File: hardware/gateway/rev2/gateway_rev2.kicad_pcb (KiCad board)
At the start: 2 copper layers, 94 x 78 mm, 68 parts, among them IC1 STM8L151K4T6, IC2 CC1101RGPR, IC5 MB85RC64TAPNF-G-BDERE1, J1 22-28-4044, J2 M20-9770342, U1 IRM-01-3.3, Y1 NX3225GA-26MHZ-TI

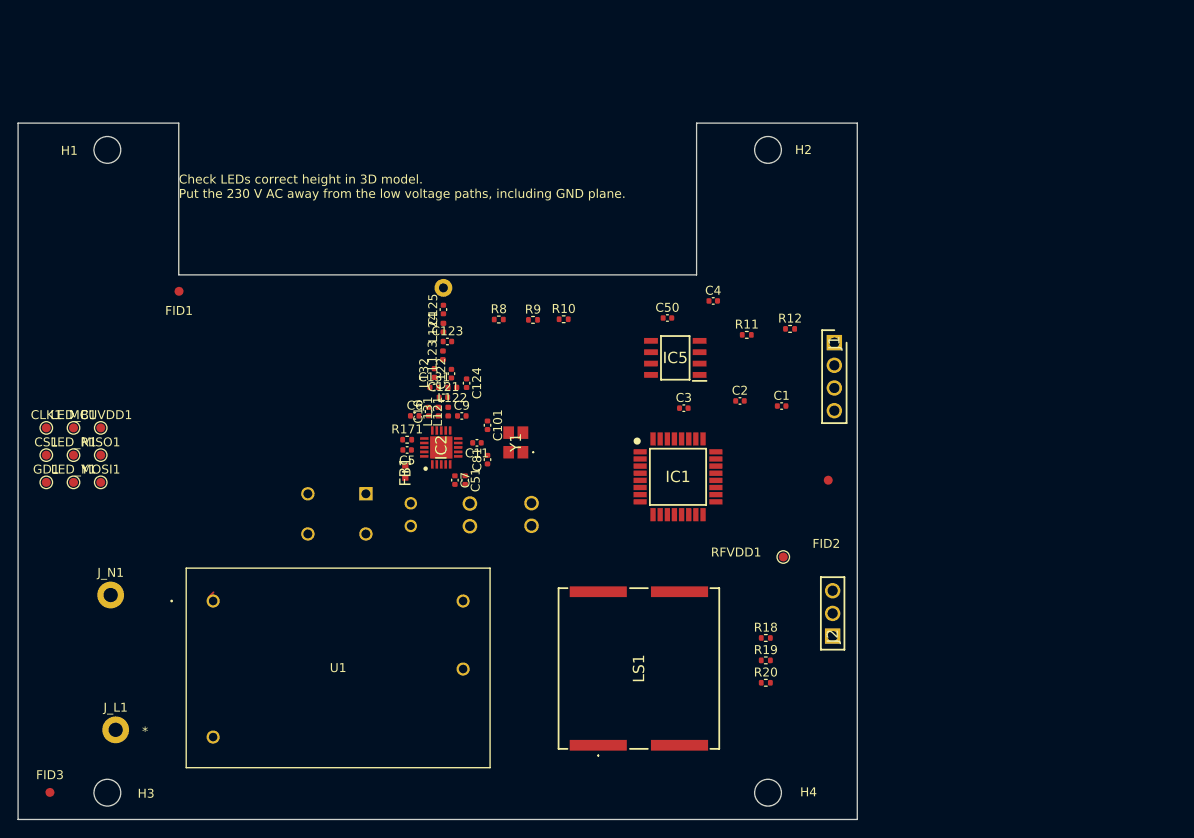
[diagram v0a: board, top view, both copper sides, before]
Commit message: EG-59 RF connected.
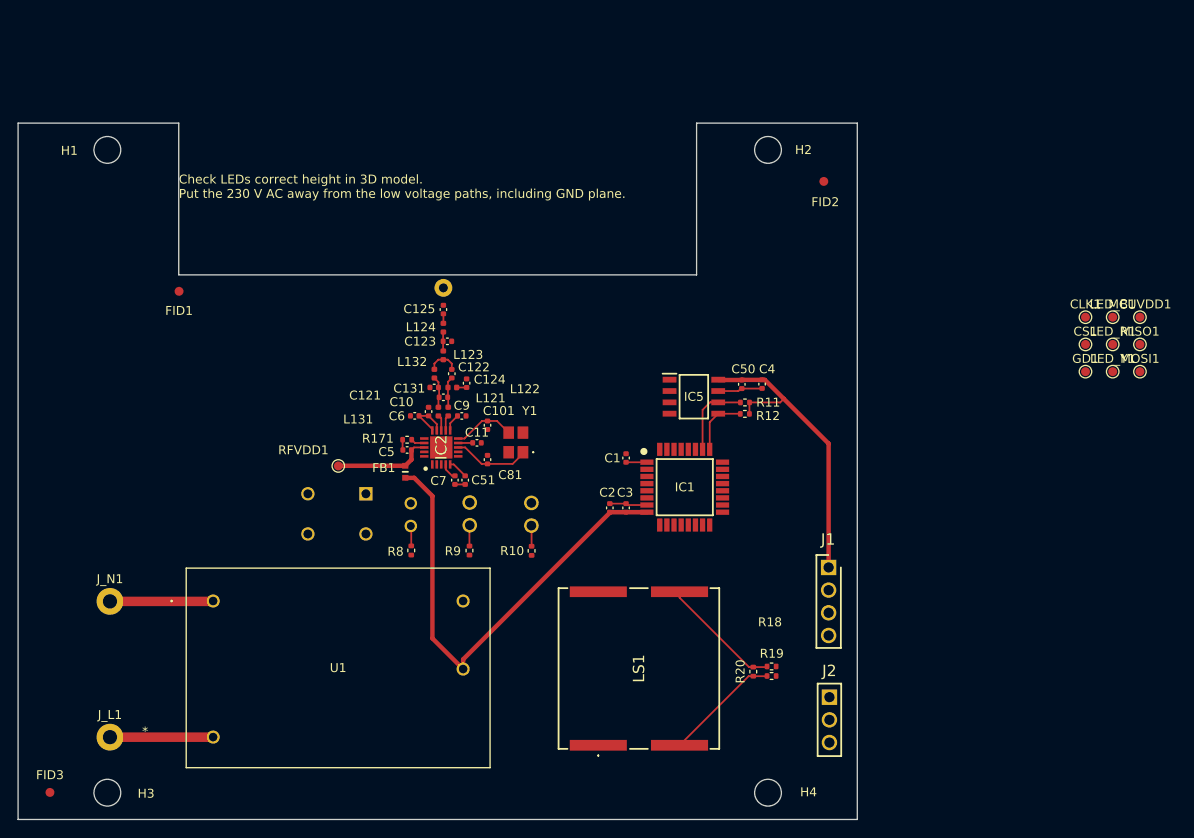
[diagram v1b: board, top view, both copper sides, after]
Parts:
- moved MCUVDD1 117.1 mm to (305.7, 101.7)
- moved MISO1 117.1 mm to (305.7, 104.8)
- moved MOSI1 117.1 mm to (305.7, 107.8)
- moved CLK1 117.1 mm to (299.6, 101.7)
- moved LED_B1 117.1 mm to (302.6, 101.7)
- moved CS1 117.1 mm to (299.6, 104.8)
- moved GD1 117.1 mm to (299.6, 107.8)
- moved LED_R1 117.1 mm to (302.6, 104.8)
- moved LED_Y1 117.1 mm to (302.6, 107.8)
- moved RFVDD1 50.9 mm to (215.9, 118.4)
- moved FID2 33.5 mm to (270.2, 86.5)
- moved R8 27.7 mm to (224.0, 127.9), turned to 90 degrees
- moved R9 26.8 mm to (230.6, 127.9), turned to 90 degrees
- moved R10 26.2 mm to (237.5, 127.9), turned to 90 degrees
- moved J1 25.2 mm to (270.8, 129.8)
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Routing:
- net VDD: track 0.00 -> 87.7 mm
- net RF_VDD: track 0.00 -> 21.9 mm
- net Net-(LS1--_1): track 0.00 -> 13.7 mm
- net Net-(LS1-+_1): track 0.00 -> 13.0 mm
- net GND: track 0.00 -> 11.6 mm
- net Net-(J_L1-V): track 0.00 -> 11.6 mm
- net Net-(J_N1-V): track 0.64 -> 11.6 mm
- net SCL: track 0.00 -> 9.02 mm
- net Net-(IC2-XOSC_Q1): track 0.00 -> 8.64 mm
- net Net-(IC2-XOSC_Q2): track 0.00 -> 7.01 mm
- net SDA: track 0.00 -> 6.87 mm
- net Net-(C122-Pad2): track 0.00 -> 3.61 mm
- net Net-(C121-Pad2): track 0.00 -> 3.53 mm
- net Net-(C121-Pad1): track 0.00 -> 3.49 mm
- net Net-(LED2-A): track 0.00 -> 2.34 mm
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
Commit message: EG-59 MCU almost connected to the RF chip.
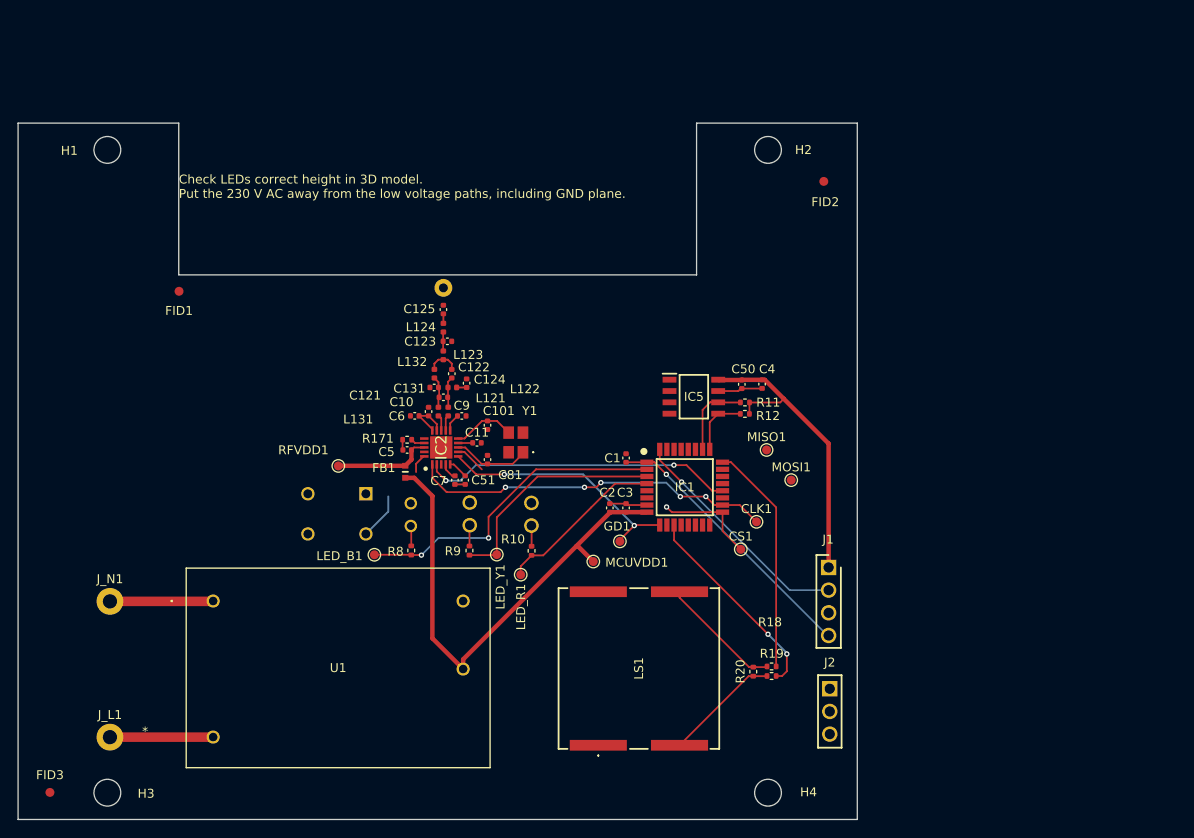
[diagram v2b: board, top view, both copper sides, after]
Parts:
- moved LED_B1 86.9 mm to (219.9, 128.3)
- moved LED_Y1 72.0 mm to (233.6, 128.3)
- moved LED_R1 71.1 mm to (236.3, 130.6)
- moved MCUVDD1 67.1 mm to (244.4, 129.1)
- moved GD1 55.5 mm to (247.4, 126.8)
- moved CS1 44.9 mm to (260.9, 127.7)
- moved MISO1 43.5 mm to (263.8, 116.6)
- moved CLK1 43.4 mm to (262.7, 124.7)
- moved MOSI1 40.9 mm to (266.6, 120.0)
- moved J2 0.94 mm to (270.9, 143.4)
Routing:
- net /MCU/SCLK: track 0.00 -> 40.7 mm, vias 0 -> 5
- net LED_B: track 0.00 -> 35.9 mm, vias 0 -> 2
- net /MCU/SDO: track 0.00 -> 35.1 mm, vias 0 -> 2
- net NRST: track 2.34 -> 30.7 mm, vias 0 -> 1
- net /MCU/IRQ: track 0.00 -> 28.2 mm, vias 0 -> 2
- net SWIM: track 0.00 -> 26.2 mm, vias 0 -> 1
- net LED_Y: track 0.00 -> 26.0 mm
- net BZR_N: track 0.00 -> 25.9 mm
- net BZR_P: track 0.00 -> 23.0 mm, vias 0 -> 2
- net LED_R: track 0.00 -> 18.9 mm
- net /MCU/CS: track 0.00 -> 15.0 mm, vias 0 -> 1
- net BTN: track 0.00 -> 5.25 mm
- net VDD: track 87.7 -> 90.3 mm
- net /MCU/SDI: track 0.00 -> 2.19 mm

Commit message: EG-59 All components connected except GND.
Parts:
- moved J1 29.2 mm to (271.4, 100.6)
- moved J2 24.6 mm to (271.4, 118.7), turned to 90 degrees
- moved CS1 0.91 mm to (261.0, 126.8)
- moved MOSI1 0.67 mm to (265.9, 120.2)
- moved MISO1 0.39 mm to (263.6, 116.9)
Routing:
- net BTN: track 5.25 -> 54.5 mm, vias 0 -> 1
- net /MCU/SDI: track 2.19 -> 44.6 mm, vias 0 -> 2
- net VDD: track 90.3 -> 125.2 mm
- net /MCU/CS: track 15.0 -> 38.0 mm, vias 1 -> 2
- net /MCU/IRQ: track 28.2 -> 5.31 mm, vias 2 -> 1
- net TX: track 0.00 -> 18.5 mm, vias 0 -> 1
- net RX: track 0.00 -> 18.2 mm, vias 0 -> 1
- net /MCU/SDO: track 35.1 -> 42.4 mm
- net NRST: track 30.7 -> 28.3 mm
- net /MCU/SCLK: track 40.7 -> 40.0 mm, vias 5 -> 2
- net BZR_N: track 25.9 -> 26.2 mm, vias 0 -> 2

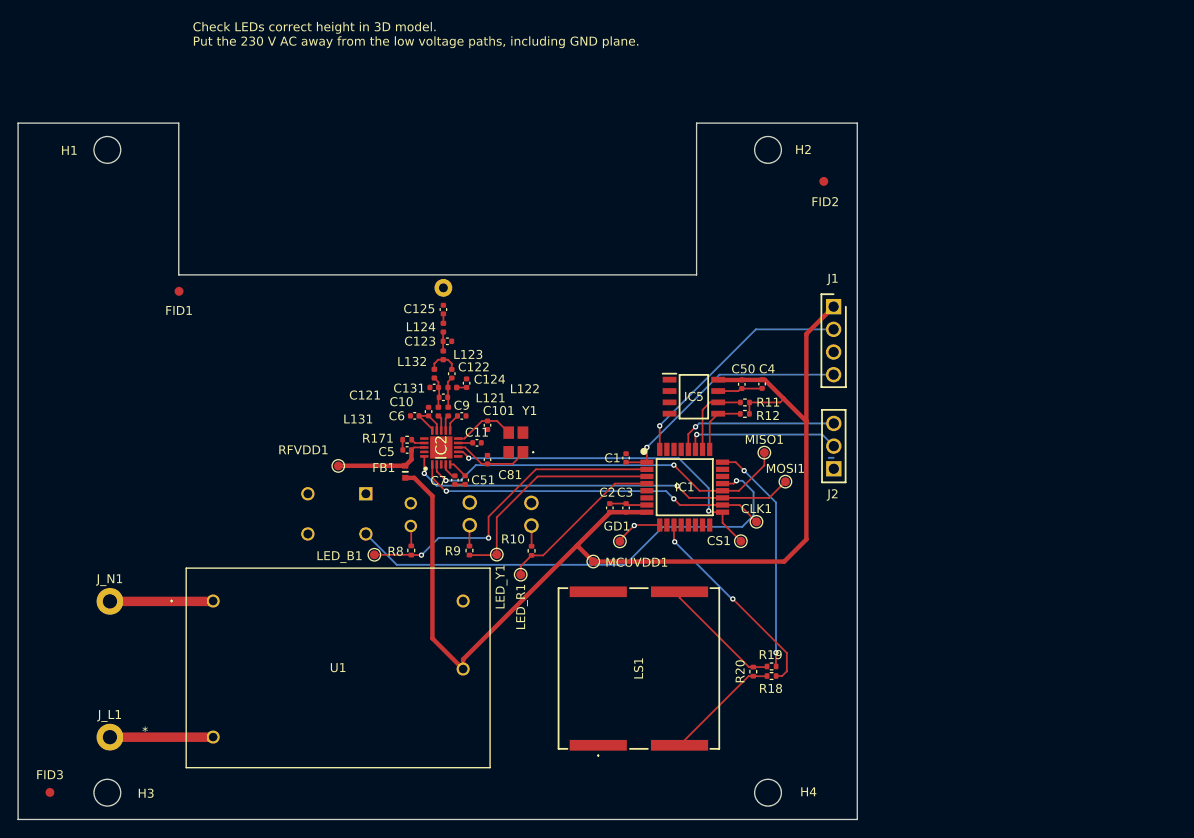
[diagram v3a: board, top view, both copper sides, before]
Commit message: EG-59 GND plane added.
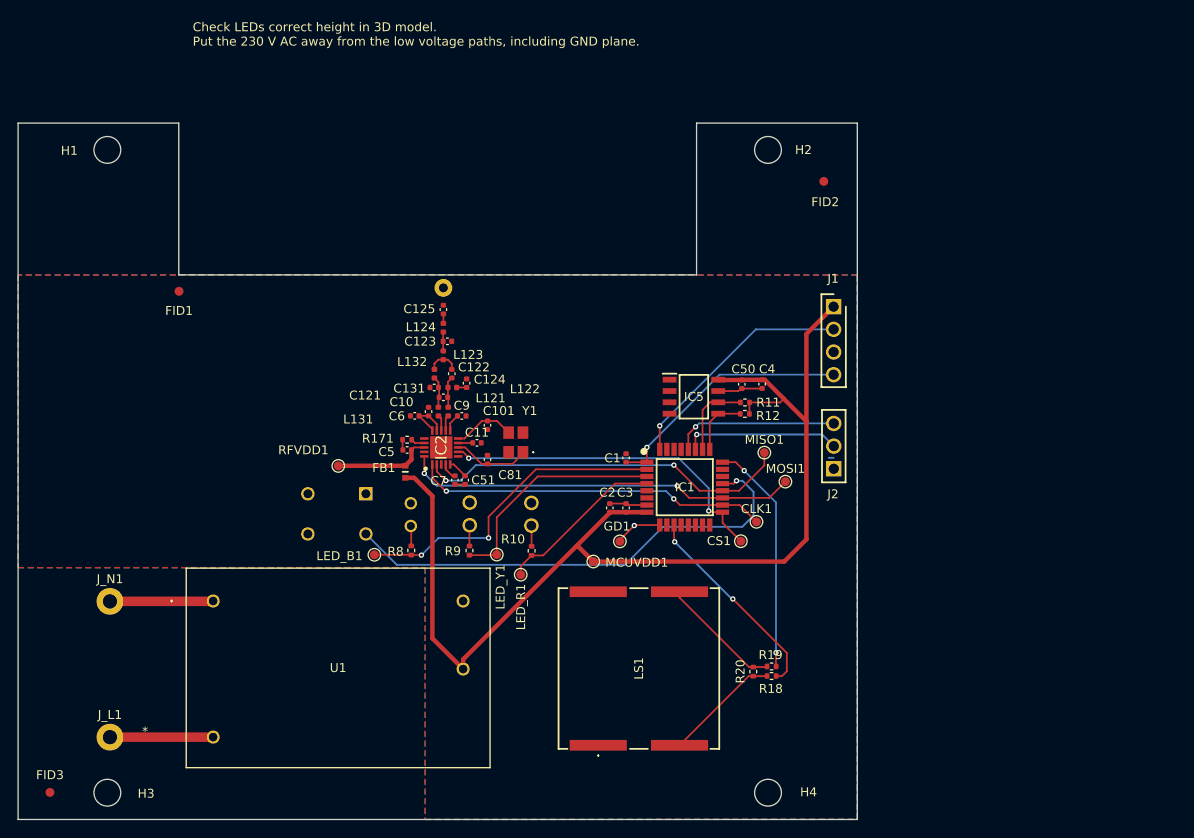
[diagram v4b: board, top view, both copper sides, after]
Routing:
- added copper zone on B.Cu, net GND
- added copper zone on F.Cu, net GND
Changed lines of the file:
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@@
 	)
 	(gr_text "Exit Guardian - Gateway REV2.0\nNPX4U 2026"
-		(at 214.91 156.55 0)
+		(at 198.03 156.69 0)
 		(layer "Edge.Cuts")
 		(effects
@@
 		(net "Net-(J_L1-V)")
 	)
+	(zone
+		(net "GND")
+		(layer "F.Cu")
+		(name "F_GND_PLANE")
+		(hatch edge 0.5)
+		(priority 1)
+		(connect_pads
+			(clearance 0.15)
+		)
+		(min_thickness 0.15)
+		(fill yes
+			(thermal_gap 0.5)
+			(thermal_bridge_width 0.5)
+			(island_removal_mode 0)
+		)
+		(polygon
+			(pts
+				(xy 274 157.99) (xy 274 97.02) (xy 180 97) (xy 180 129.79) (xy 225.6 129.78) (xy 225.61 158)
+			)
+		)
+	)
+	(zone
+		(net "GND")
+		(layer "B.Cu")
+		(name "B_GND_PLANE")
+		(hatch edge 0.5)
+		(connect_pads
+			(clearance 0.15)
+		)
+		(min_thickness 0.15)
+		(fill yes
+			(thermal_gap 0.5)
+			(thermal_bridge_width 0.5)
+			(island_removal_mode 0)
+		)
+		(polygon
+			(pts
+				(xy 273.98 157.99) (xy 274.01 97.12) (xy 274.01 97.02) (xy 180 97) (xy 180 129.79) (xy 225.6 129.82)
+				(xy 225.61 158)
+			)
+		)
+	)
 	(embedded_fonts no)

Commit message: EG-59 No DRC Errors. All connected. Still warnings.
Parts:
- moved C5 0.71 mm to (222.9, 116.6)
- moved R171 0.71 mm to (222.9, 115.5)
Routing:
- net RF_VDD: track 21.9 -> 46.7 mm, vias 0 -> 5
- net /MCU/IRQ: track 5.31 -> 28.2 mm, vias 1 -> 4
- net Net-(LS1--_1): track 13.7 -> 22.8 mm
- net Net-(LS1-+_1): track 13.0 -> 22.1 mm
- net Net-(ANT1-ANT): track 0.00 -> 1.95 mm
- net /MCU/CS: track 38.0 -> 39.5 mm
- net GND: track 11.6 -> 13.1 mm, vias 0 -> 5
- net Net-(IC2-RBIAS): track 1.56 -> 2.26 mm
- net LED_Y: track 26.0 -> 26.6 mm
- net RX: track 18.2 -> 17.6 mm
- net LED_B: track 35.9 -> 36.4 mm
